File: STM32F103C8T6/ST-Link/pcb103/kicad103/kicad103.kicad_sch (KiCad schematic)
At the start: 21 parts, among them IC1 LD1117DT33TR, J1 0480372200, J2 Conn_01x02_Socket, U1 STM32F103C8T6, Y1 8MHz 20pF

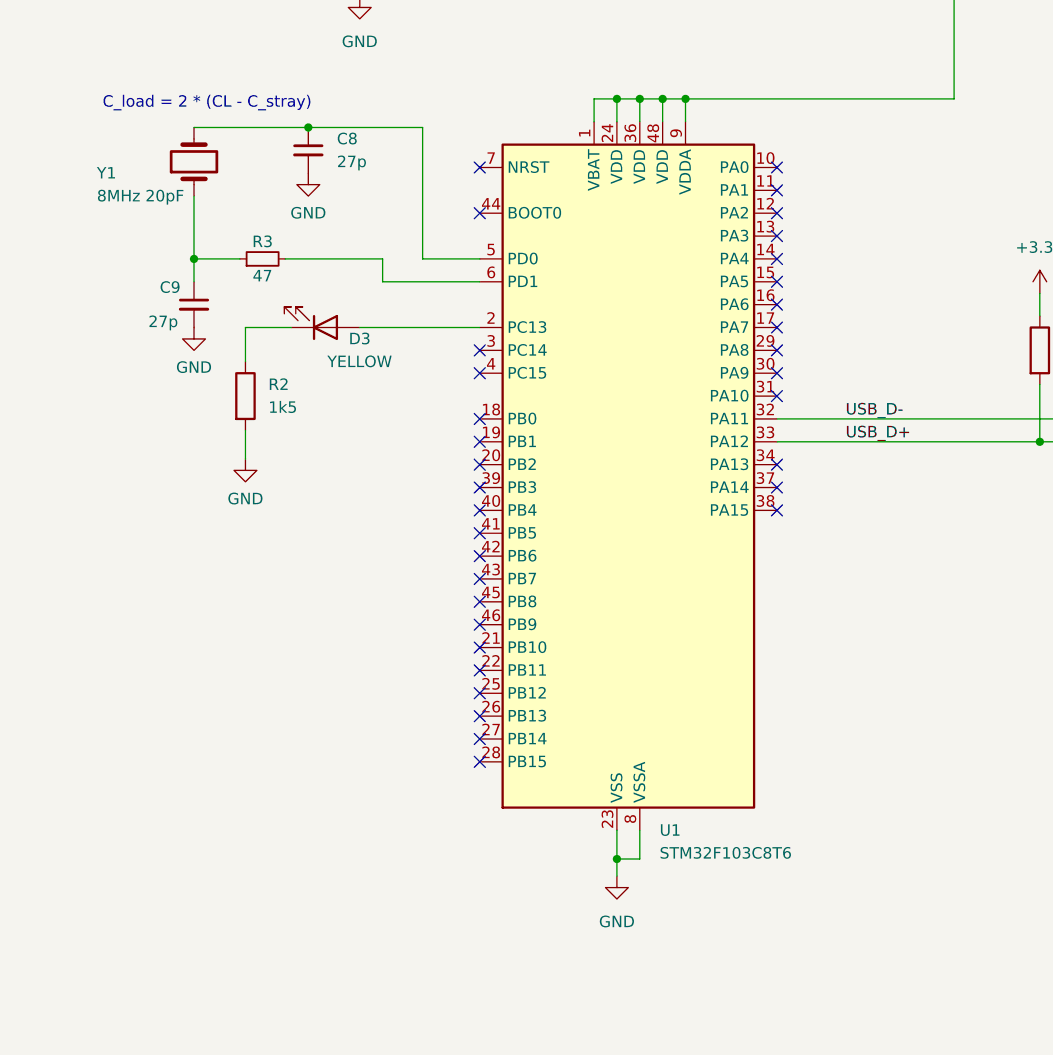
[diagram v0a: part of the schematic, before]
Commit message: Add JTAG
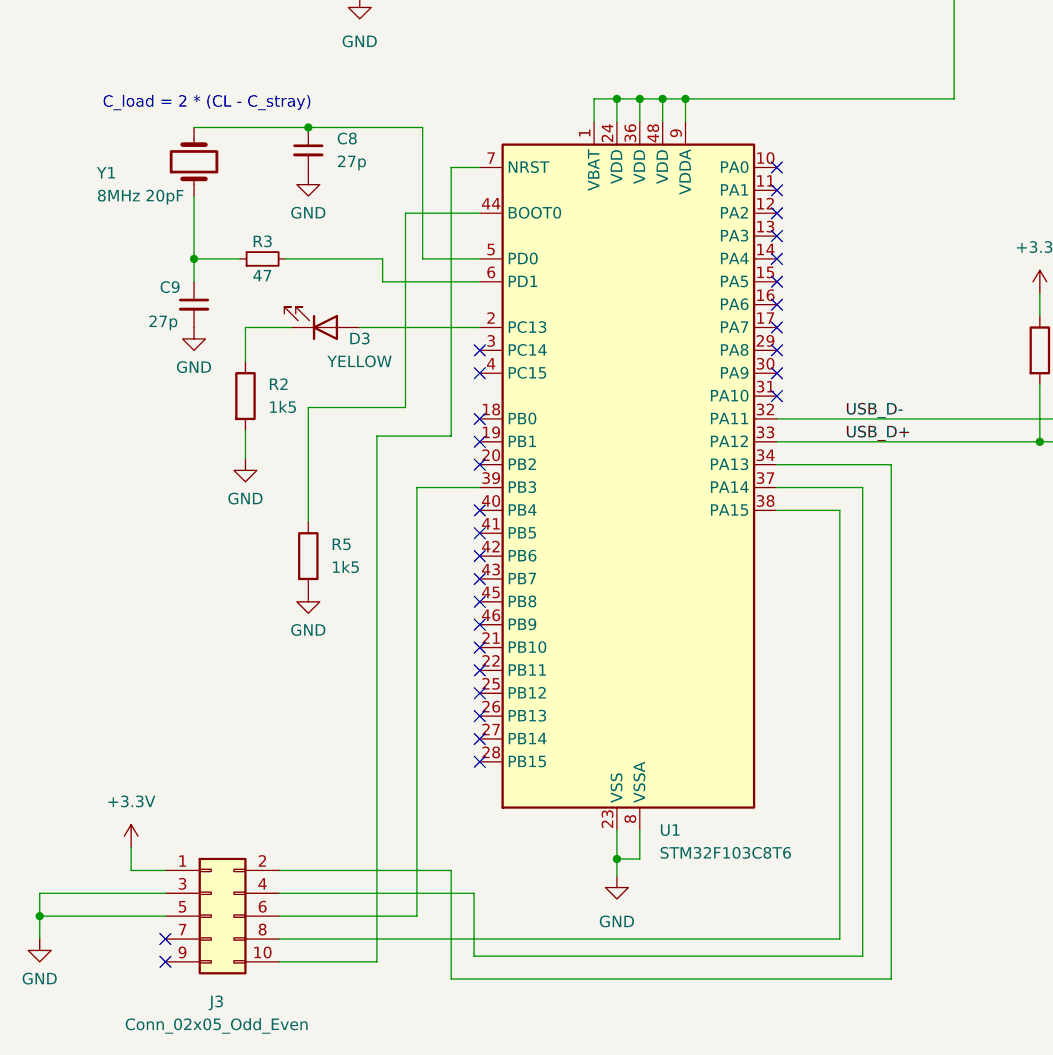
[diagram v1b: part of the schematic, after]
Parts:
- added J3: Conn_02x05_Odd_Even, Connector_PinHeader_1.27mm:PinHeader_2x05_P1.27mm_Vertical_SMD, symbol Connector_Generic:Conn_02x05_Odd_Even
- added R5: 1k5, Resistor_SMD:R_0805_2012Metric, symbol Device:R
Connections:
- net +3.3V: now also J3.1 (Pin_1)
- net GND: now also J3.3 (Pin_3), J3.5 (Pin_5), R5.2
- net at U1.34 (PA13): now also J3.2 (Pin_2)
- net at U1.37 (PA14): now also J3.4 (Pin_4)
- net at U1.38 (PA15): now also J3.8 (Pin_8)
- net at U1.39 (PB3): now also J3.6 (Pin_6)
- net at U1.44 (BOOT0): now also R5.1
- net at U1.7 (NRST): now also J3.10 (Pin_10)
- no-connect marks 38 -> 34

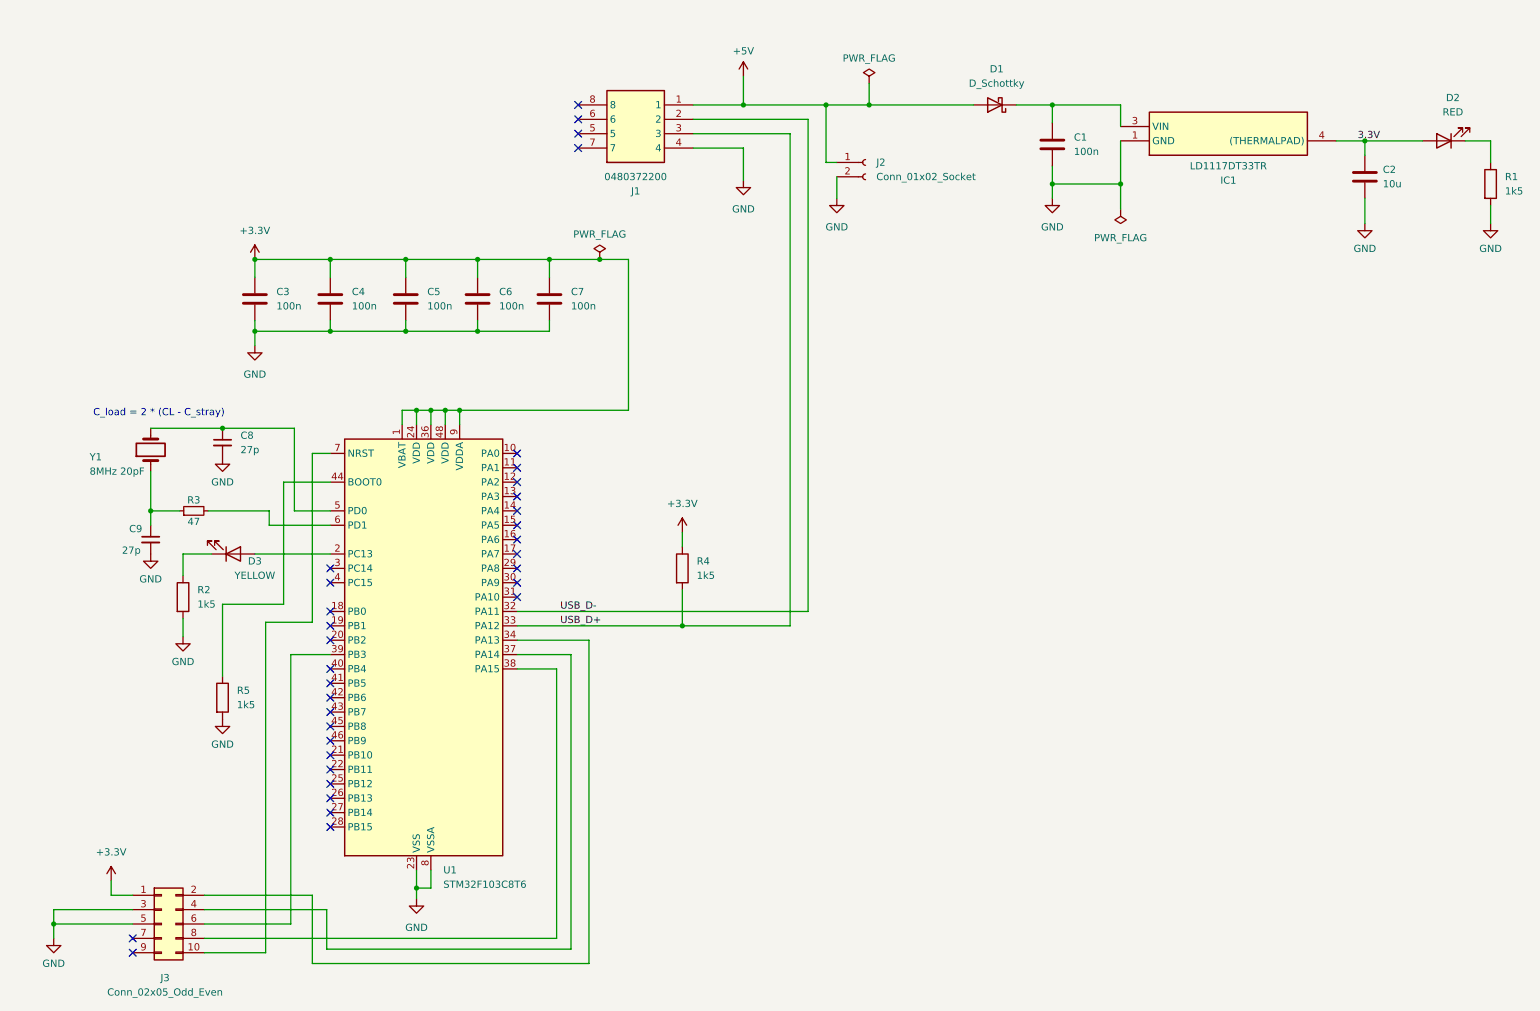
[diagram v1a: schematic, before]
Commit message: Remaining pins
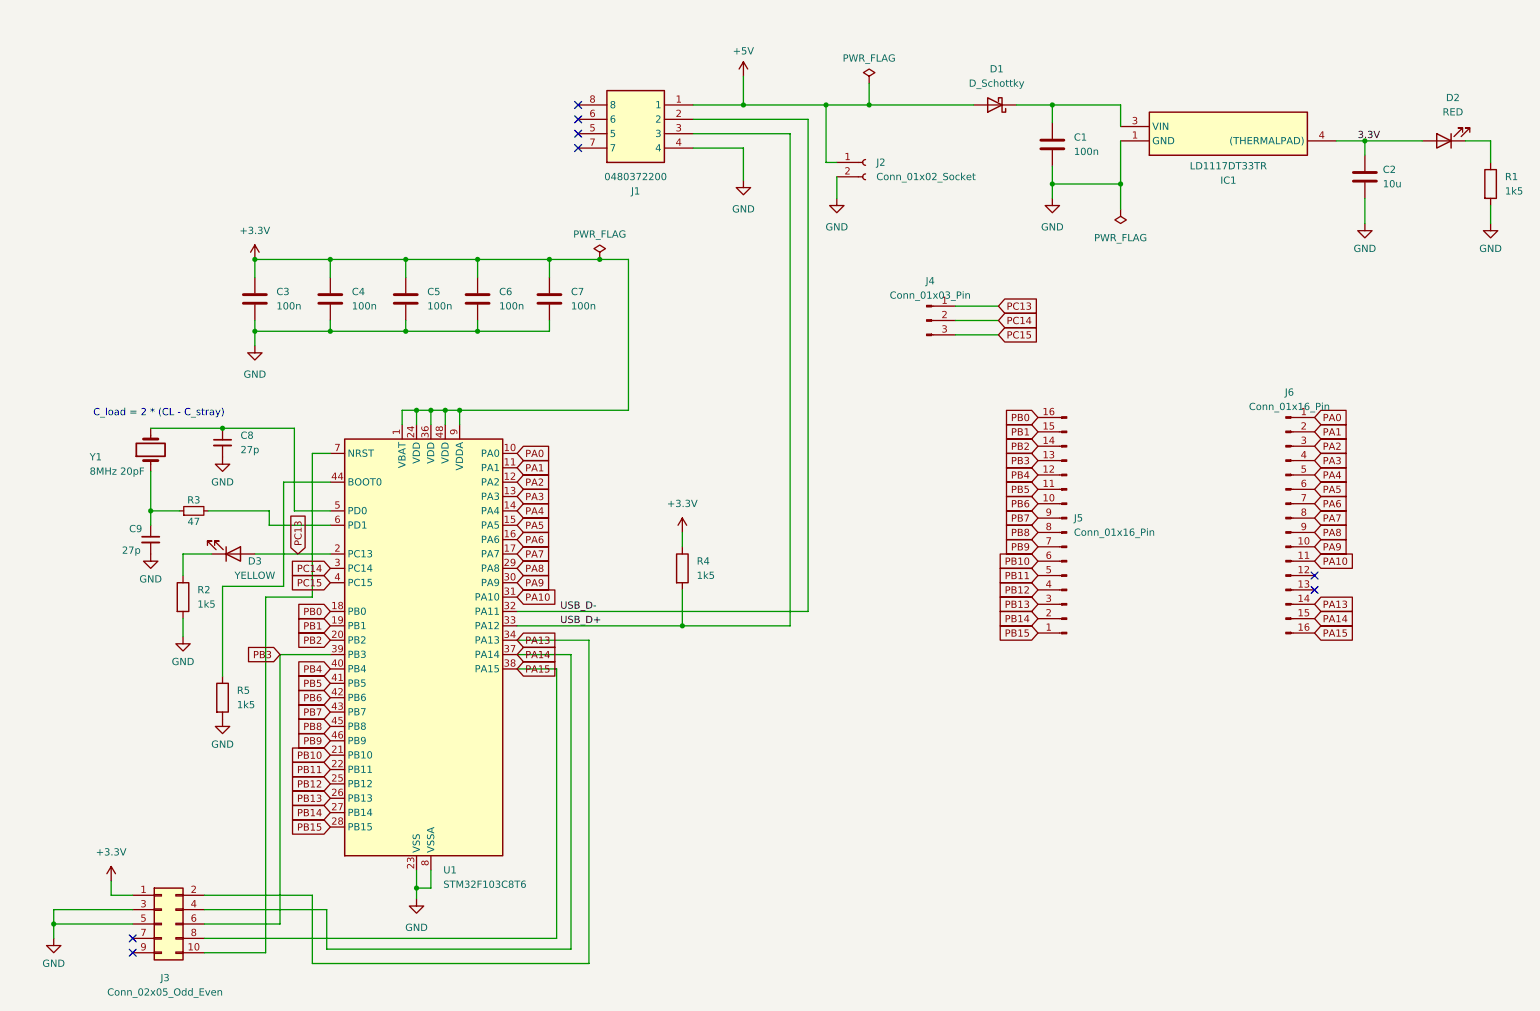
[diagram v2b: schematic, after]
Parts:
- added J4: Conn_01x03_Pin, Connector_PinHeader_2.54mm:PinHeader_1x03_P2.54mm_Vertical, symbol Connector:Conn_01x03_Pin
- added J5, J6: Conn_01x16_Pin, Connector_PinHeader_2.54mm:PinHeader_1x16_P2.54mm_Vertical, symbol Connector:Conn_01x16_Pin
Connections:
- net PA13: now reaches J3.2 (Pin_2), U1.34 (PA13)
- net PA13: now also J6.14 (Pin_14)
- net PA14: now reaches J3.4 (Pin_4), U1.37 (PA14)
- net PA14: now also J6.15 (Pin_15)
- net PB3: now reaches J3.6 (Pin_6), U1.39 (PB3)
- net PB3: now also J5.13 (Pin_13)
- net PA15: now reaches J3.8 (Pin_8), U1.38 (PA15)
- net PA15: now also J6.16 (Pin_16)
- net PC13: now reaches D3.2 (A), U1.2 (PC13)
- net PC13: now also J4.1 (Pin_1)
- net PA0: now reaches U1.10 (PA0)
- net PA0: now also J6.1 (Pin_1)
- net PA1: now reaches U1.11 (PA1)
- net PA1: now also J6.2 (Pin_2)
- net PA2: now reaches U1.12 (PA2)
- net PA2: now also J6.3 (Pin_3)
- net PA3: now reaches U1.13 (PA3)
- net PA3: now also J6.4 (Pin_4)
- net PA4: now reaches U1.14 (PA4)
- net PA4: now also J6.5 (Pin_5)
- net PA5: now reaches U1.15 (PA5)
- net PA5: now also J6.6 (Pin_6)
- net PA6: now reaches U1.16 (PA6)
- net PA6: now also J6.7 (Pin_7)
- net PA7: now reaches U1.17 (PA7)
- net PA7: now also J6.8 (Pin_8)
- net PB0: now reaches U1.18 (PB0)
- net PB0: now also J5.16 (Pin_16)
- net PB1: now reaches U1.19 (PB1)
- net PB1: now also J5.15 (Pin_15)
- net PB2: now reaches U1.20 (PB2)
- net PB2: now also J5.14 (Pin_14)
- net PB10: now reaches U1.21 (PB10)
- net PB10: now also J5.6 (Pin_6)
- net PB11: now reaches U1.22 (PB11)
- net PB11: now also J5.5 (Pin_5)
- net PB12: now reaches U1.25 (PB12)
- net PB12: now also J5.4 (Pin_4)
- net PB13: now reaches U1.26 (PB13)
- net PB13: now also J5.3 (Pin_3)
- net PB14: now reaches U1.27 (PB14)
- net PB14: now also J5.2 (Pin_2)
- net PB15: now reaches U1.28 (PB15)
- net PB15: now also J5.1 (Pin_1)
- net PA8: now reaches U1.29 (PA8)
- net PA8: now also J6.9 (Pin_9)
- net PC14: now reaches U1.3 (PC14)
- net PC14: now also J4.2 (Pin_2)
- net PA9: now reaches U1.30 (PA9)
- net PA9: now also J6.10 (Pin_10)
- net PA10: now reaches U1.31 (PA10)
- net PA10: now also J6.11 (Pin_11)
- net PC15: now reaches U1.4 (PC15)
- net PC15: now also J4.3 (Pin_3)
- net PB4: now reaches U1.40 (PB4)
- net PB4: now also J5.12 (Pin_12)
- net PB5: now reaches U1.41 (PB5)
- net PB5: now also J5.11 (Pin_11)
- net PB6: now reaches U1.42 (PB6)
- net PB6: now also J5.10 (Pin_10)
- net PB7: now reaches U1.43 (PB7)
- net PB7: now also J5.9 (Pin_9)
- net PB8: now reaches U1.45 (PB8)
- net PB8: now also J5.8 (Pin_8)
- net PB9: now reaches U1.46 (PB9)
- net PB9: now also J5.7 (Pin_7)
- no-connect marks 34 -> 8

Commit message: SWO/SWD
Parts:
- added J7: Conn_01x04_Pin, Connector_PinHeader_2.54mm:PinHeader_1x04_P2.54mm_Vertical, symbol Connector:Conn_01x04_Pin
- added J8: Conn_01x05_Socket, Connector_PinSocket_2.54mm:PinSocket_1x05_P2.54mm_Vertical, symbol Connector:Conn_01x05_Socket
- added R6: 220, symbol Device:R
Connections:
- net +3.3V: now also D2.1 (K), R1.1, J7.1 (Pin_1), J8.2 (Pin_2)
- net GND: now also J7.4 (Pin_4), J8.5 (Pin_5)
- net PA13: now also J8.3 (Pin_3)
- net PA14: now also J8.4 (Pin_4)
- net PB12: now also R6.2
- net PB13: now also J7.3 (Pin_3)
- net PB14: now also J7.2 (Pin_2), R6.1
- net PB3: now also J8.1 (Pin_1)

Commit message: SWD 220R
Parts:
- R6: footprint (none) -> Resistor_SMD:R_1206_3216Metric

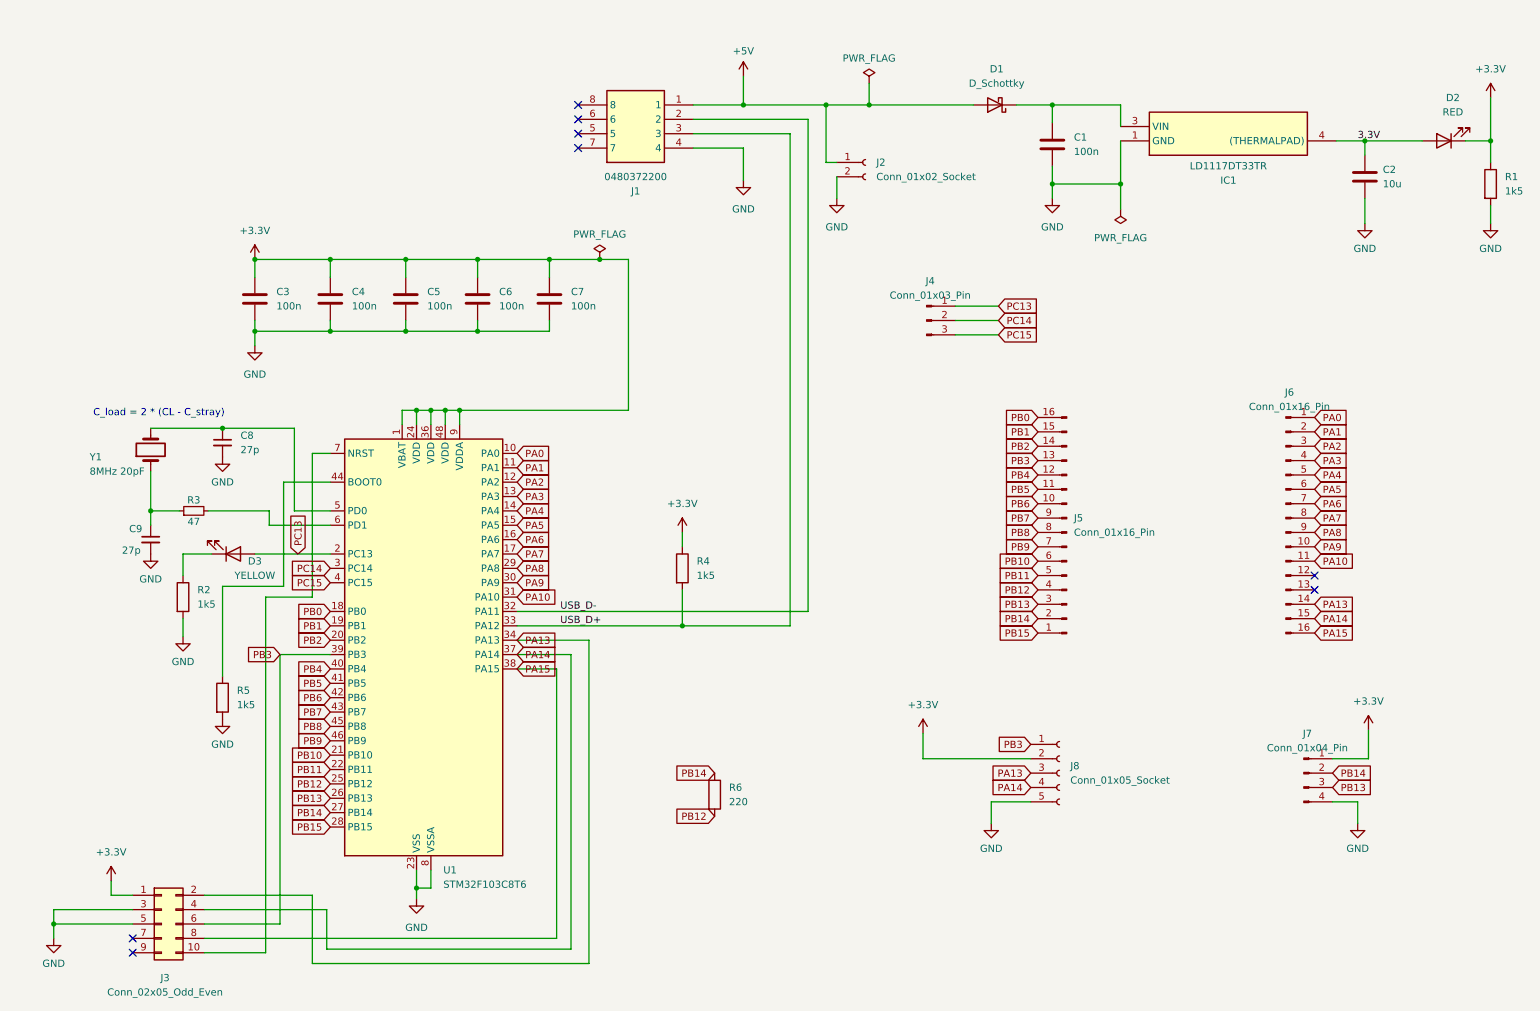
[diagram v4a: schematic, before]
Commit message: Mounting holes
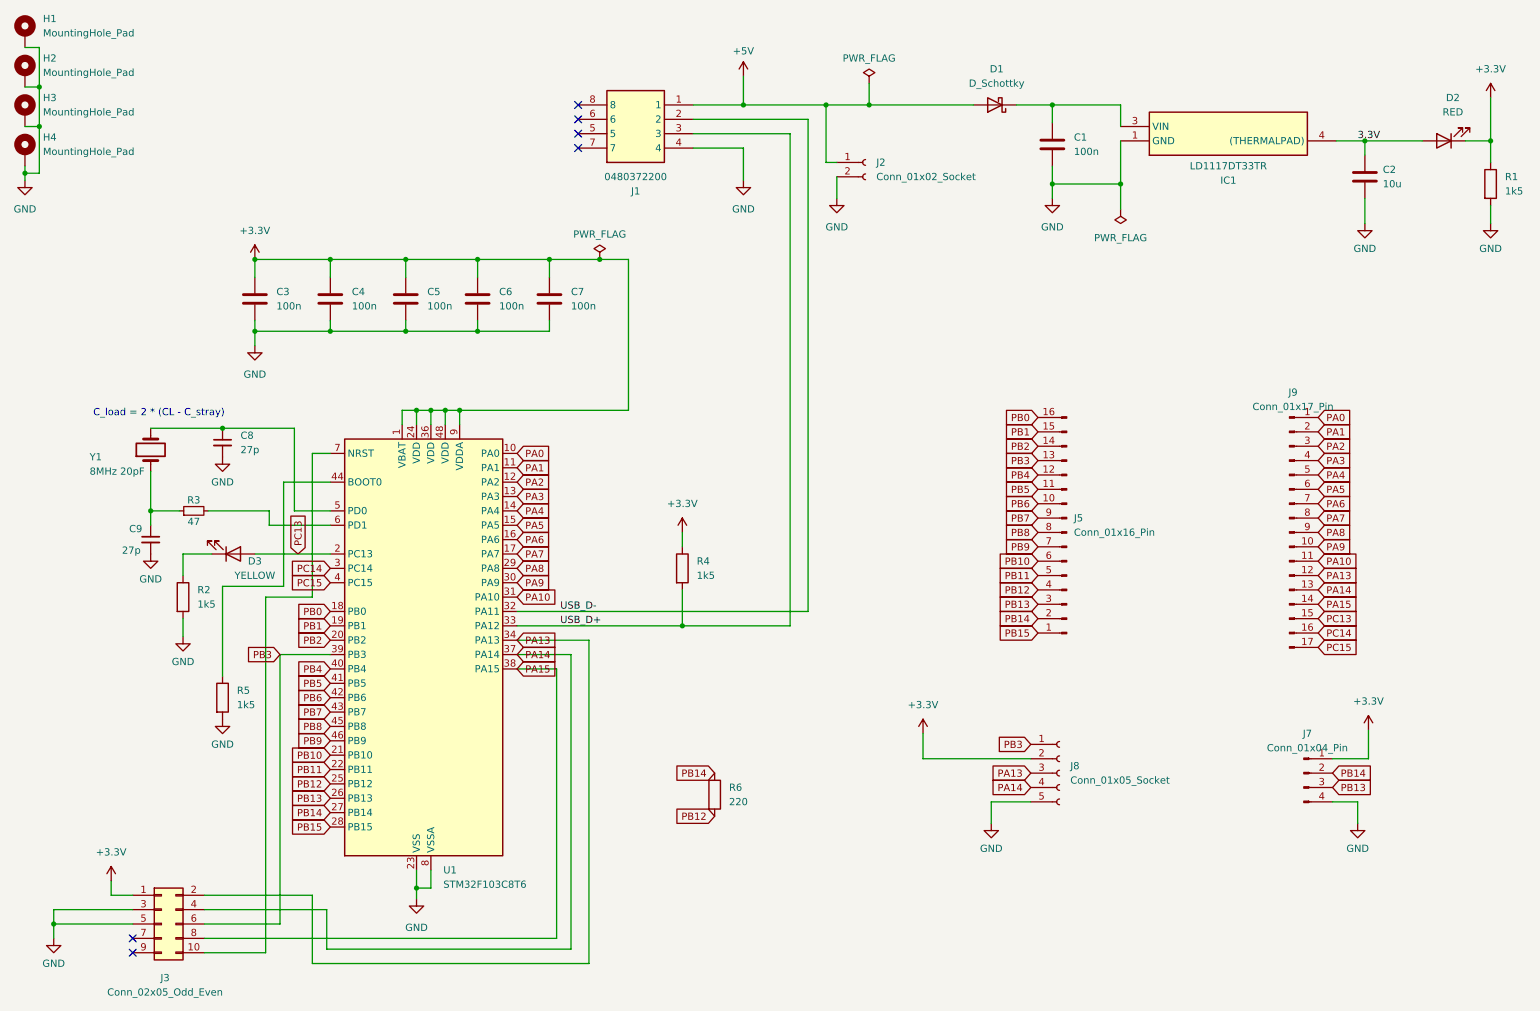
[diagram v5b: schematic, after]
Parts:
- removed J4: Conn_01x03_Pin, Connector_PinHeader_2.54mm:PinHeader_1x03_P2.54mm_Vertical, symbol Connector:Conn_01x03_Pin
- removed J6: Conn_01x16_Pin, Connector_PinHeader_2.54mm:PinHeader_1x16_P2.54mm_Vertical, symbol Connector:Conn_01x16_Pin
- added H1, H2, H3, H4: MountingHole_Pad, MountingHole:MountingHole_4.3mm_M4_Pad_Via, symbol Mechanical:MountingHole_Pad
- added J9: Conn_01x17_Pin, Connector_PinHeader_2.54mm:PinHeader_1x17_P2.54mm_Vertical, symbol Connector:Conn_01x17_Pin
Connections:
- net GND: now also H1.1, H2.1, H3.1, H4.1
- net PA0: now also J9.1 (Pin_1)
- net PA1: now also J9.2 (Pin_2)
- net PA10: now also J9.11 (Pin_11)
- net PA13: now also J9.12 (Pin_12)
- net PA14: now also J9.13 (Pin_13)
- net PA15: now also J9.14 (Pin_14)
- net PA2: now also J9.3 (Pin_3)
- net PA3: now also J9.4 (Pin_4)
- net PA4: now also J9.5 (Pin_5)
- net PA5: now also J9.6 (Pin_6)
- net PA6: now also J9.7 (Pin_7)
- net PA7: now also J9.8 (Pin_8)
- net PA8: now also J9.9 (Pin_9)
- net PA9: now also J9.10 (Pin_10)
- net PC13: now also J9.15 (Pin_15)
- net PC14: now also J9.16 (Pin_16)
- net PC15: now also J9.17 (Pin_17)
- no-connect marks 8 -> 6
